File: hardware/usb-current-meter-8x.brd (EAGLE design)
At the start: 94 x 44.5 mm, 154 parts, among them IC10 OPA2234U, IC12 LTC485S, IC2 OPA2234U, IC3 MEGA48/88/168-AU, IC4 OPA2234U, IC5 OPA2234U, IC6 OPA2234U, IC7 OPA2234U, IC8 OPA2234U, IC9 OPA2234U, U3 RJ45-8PTH, X1 MC2, X2 MC2, X3 MC2, X4 MC2, X5 MC2, X6 MC2, X7 MC2, X8 MC2

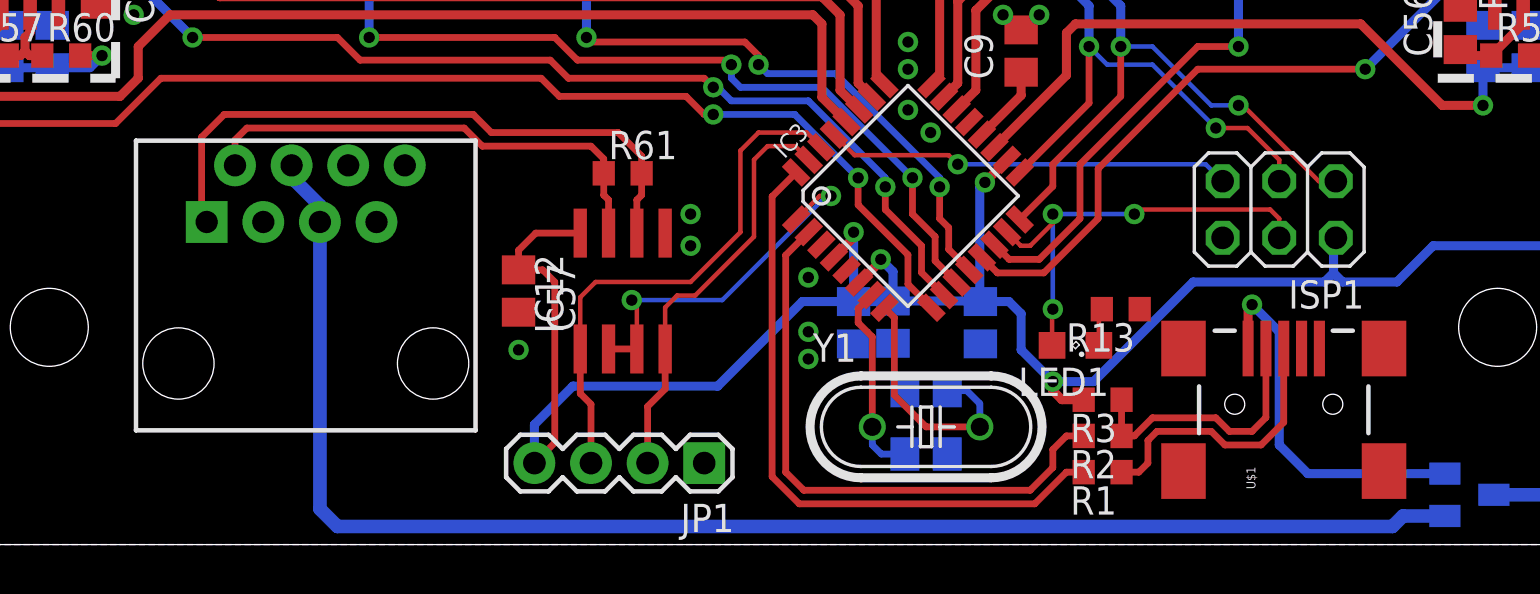
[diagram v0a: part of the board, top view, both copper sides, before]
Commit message: hw: move low-side connector .6mm out
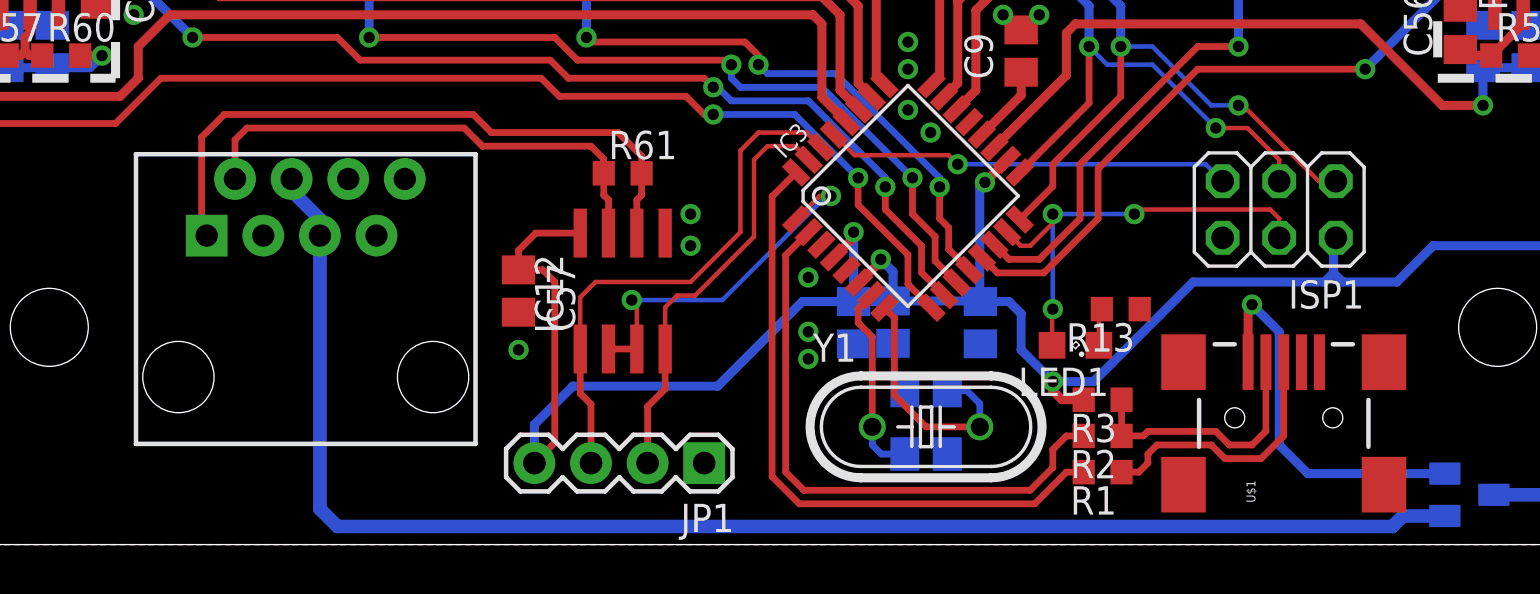
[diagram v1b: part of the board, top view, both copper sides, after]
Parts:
- moved U3 0.61 mm to (26.0, 7.52)
- moved U$1 0.61 mm to (69.9, 5.69)
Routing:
- net VIN_USB: track 16.8 -> 17.4 mm
- net VIN_BUS: track 67.0 -> 66.3 mm
- net N$2: track 12.6 -> 12.0 mm
- net 485_P: track 28.4 -> 29.0 mm
- net 485_N: track 21.9 -> 22.5 mm
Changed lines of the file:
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@@
 <?xml version="1.0" encoding="utf-8"?>
 <!DOCTYPE eagle SYSTEM "eagle.dtd">
-<eagle version="6.1">
+<eagle version="6.2">
 <drawing>
 <settings>
@@
 <element name="R13" library="rcl" package="R0603" value="330" x="62.5856" y="10.5664" rot="R180"/>
 <element name="ISP1" library="balto" package="2X03" value="" x="69.6976" y="15.0368" rot="R180"/>
-<element name="U$1" library="SparkFun" package="USB-MINIB" value="USB-MINIB-5PIN" x="69.9008" y="6.2992" rot="R90"/>
+<element name="U$1" library="SparkFun" package="USB-MINIB" value="USB-MINIB-5PIN" x="69.9008" y="5.6896" rot="R90"/>
 <element name="Y1" library="SparkFun" package="HC49U-V" value="" x="53.848" y="5.2832"/>
 <element name="C9" library="rcl" package="C0805" value=".1u" x="58.1152" y="22.1488" rot="R90"/>
@@
 <element name="C57" library="rcl" package="C0805" value=".1u" x="35.56" y="11.3792" rot="R270"/>
 <element name="R61" library="rcl" package="R0603" value="120" x="40.2336" y="16.6624"/>
-<element name="U3" library="SparkFun-Connectors" package="RJ45-8" value="RJ45-8PTH" x="26.0096" y="8.128"/>
+<element name="U3" library="SparkFun-Connectors" package="RJ45-8" value="RJ45-8PTH" x="26.0096" y="7.5184"/>
 <element name="BOX1" library="hammond" package="1591XXA" value="HAMMOND-BOX-XXA" x="0" y="0"/>
 <element name="D9" library="diode" package="SOT23" value="BAT54C" x="78.232" y="2.2352" rot="MR90"/>
@@
 <contactref element="R3" pad="1"/>
 <contactref element="U$1" pad="D-"/>
-<wire x1="64.008" y1="5.6896" x2="66.8528" y2="5.6896" width="0.3048" layer="1"/>
-<wire x1="66.8528" y1="5.6896" x2="67.4624" y2="5.08" width="0.3048" layer="1"/>
-<wire x1="67.4624" y1="5.08" x2="68.4784" y2="5.08" width="0.3048" layer="1"/>
-<wire x1="68.4784" y1="5.08" x2="69.1008" y2="5.7024" width="0.3048" layer="1"/>
-<wire x1="69.1008" y1="8.7992" x2="69.1008" y2="5.7024" width="0.3048" layer="1"/>
+<wire x1="63.8048" y1="5.08" x2="66.8528" y2="5.08" width="0.3048" layer="1"/>
+<wire x1="66.8528" y1="5.08" x2="67.4624" y2="4.4704" width="0.3048" layer="1"/>
+<wire x1="67.4624" y1="4.4704" x2="68.4784" y2="4.4704" width="0.3048" layer="1"/>
+<wire x1="68.4784" y1="4.4704" x2="69.1008" y2="5.0928" width="0.3048" layer="1"/>
+<wire x1="69.1008" y1="8.1896" x2="69.1008" y2="5.0928" width="0.3048" layer="1"/>
 <wire x1="62.6228" y1="4.8768" x2="62.6228" y2="6.5024" width="0.3048" layer="1"/>
-<wire x1="62.6228" y1="4.8768" x2="63.1952" y2="4.8768" width="0.3048" layer="1"/>
-<wire x1="63.1952" y1="4.8768" x2="64.008" y2="5.6896" width="0.3048" layer="1"/>
+<wire x1="62.6228" y1="4.8768" x2="63.6016" y2="4.8768" width="0.3048" layer="1"/>
+<wire x1="63.6016" y1="4.8768" x2="63.8048" y2="5.08" width="0.3048" layer="1"/>
 </signal>
 <signal name="N$2">
 <contactref element="R1" pad="1"/>
 <contactref element="U$1" pad="D+"/>
-<wire x1="64.2112" y1="5.08" x2="66.6496" y2="5.08" width="0.3048" layer="1"/>
-<wire x1="66.6496" y1="5.08" x2="67.2592" y2="4.4704" width="0.3048" layer="1"/>
-<wire x1="67.2592" y1="4.4704" x2="68.8848" y2="4.4704" width="0.3048" layer="1"/>
-<wire x1="68.8848" y1="4.4704" x2="69.9008" y2="5.4864" width="0.3048" layer="1"/>
-<wire x1="69.9008" y1="8.7992" x2="69.9008" y2="5.4864" width="0.3048" layer="1"/>
-<wire x1="64.2112" y1="5.08" x2="63.8048" y2="4.6736" width="0.3048" layer="1"/>
-<wire x1="63.8048" y1="4.6736" x2="63.8048" y2="3.6576" width="0.3048" layer="1"/>
+<wire x1="64.2112" y1="4.4704" x2="66.6496" y2="4.4704" width="0.3048" layer="1"/>
+<wire x1="66.6496" y1="4.4704" x2="67.2592" y2="3.8608" width="0.3048" layer="1"/>
+<wire x1="67.2592" y1="3.8608" x2="68.8848" y2="3.8608" width="0.3048" layer="1"/>
+<wire x1="68.8848" y1="3.8608" x2="69.9008" y2="4.8768" width="0.3048" layer="1"/>
+<wire x1="69.9008" y1="8.1896" x2="69.9008" y2="4.8768" width="0.3048" layer="1"/>
+<wire x1="64.2112" y1="4.4704" x2="63.8048" y2="4.064" width="0.3048" layer="1"/>
+<wire x1="63.8048" y1="4.064" x2="63.8048" y2="3.6576" width="0.3048" layer="1"/>
 <wire x1="63.8048" y1="3.6576" x2="63.3984" y2="3.2512" width="0.3048" layer="1"/>
 <wire x1="63.3984" y1="3.2512" x2="62.6228" y2="3.2512" width="0.3048" layer="1"/>
@@
 <wire x1="33.528" y1="19.304" x2="22.352" y2="19.304" width="0.3048" layer="1"/>
 <wire x1="22.352" y1="19.304" x2="21.336" y2="18.288" width="0.3048" layer="1"/>
-<wire x1="21.336" y1="18.288" x2="21.336" y2="14.7066" width="0.3048" layer="1"/>
-<wire x1="21.336" y1="14.7066" x2="21.5646" y2="14.478" width="0.3048" layer="1"/>
+<wire x1="21.336" y1="18.288" x2="21.336" y2="14.097" width="0.3048" layer="1"/>
+<wire x1="21.336" y1="14.097" x2="21.5646" y2="13.8684" width="0.3048" layer="1"/>
 </signal>
 <signal name="485_N">
@@
 <wire x1="33.1216" y1="18.6944" x2="23.368" y2="18.6944" width="0.3048" layer="1"/>
 <wire x1="23.368" y1="18.6944" x2="22.8346" y2="18.161" width="0.3048" layer="1"/>
-<wire x1="22.8346" y1="17.018" x2="22.8346" y2="18.161" width="0.3048" layer="1"/>
+<wire x1="22.8346" y1="16.4084" x2="22.8346" y2="18.161" width="0.3048" layer="1"/>
 </signal>
 <signal name="VIN_BUS">
 <contactref element="U3" pad="4"/>
 <contactref element="U3" pad="5"/>
-<wire x1="26.6446" y1="14.478" x2="26.6446" y2="1.6002" width="0.6096" layer="16"/>
+<wire x1="26.6446" y1="13.8684" x2="26.6446" y2="1.6002" width="0.6096" layer="16"/>
 <wire x1="26.6446" y1="1.6002" x2="27.432" y2="0.8128" width="0.6096" layer="16"/>
 <wire x1="27.432" y1="0.8128" x2="74.7776" y2="0.8128" width="0.6096" layer="16"/>
@@
 <wire x1="74.7776" y1="0.8128" x2="75.25" y2="1.2852" width="0.6096" layer="16"/>
 <wire x1="77.132" y1="1.2852" x2="75.25" y2="1.2852" width="0.6096" layer="16"/>
-<wire x1="26.6446" y1="14.478" x2="26.6446" y2="15.2146" width="0.6096" layer="16"/>
-<wire x1="25.3746" y1="17.018" x2="25.3746" y2="16.4846" width="0.6096" layer="16"/>
-<wire x1="25.3746" y1="16.4846" x2="26.6446" y2="15.2146" width="0.6096" layer="16"/>
+<wire x1="26.6446" y1="13.8684" x2="26.6446" y2="14.605" width="0.6096" layer="16"/>
+<wire x1="25.3746" y1="16.4084" x2="25.3746" y2="15.875" width="0.6096" layer="16"/>
+<wire x1="25.3746" y1="15.875" x2="26.6446" y2="14.605" width="0.6096" layer="16"/>
 </signal>
 <signal name="VIN_USB">
 <contactref element="U$1" pad="VBUS"/>
 <contactref element="D9" pad="2"/>
-<wire x1="68.3008" y1="8.7992" x2="68.3008" y2="10.592" width="0.4064" layer="1"/>
+<wire x1="68.3008" y1="8.1896" x2="68.3008" y2="10.592" width="0.4064" layer="1"/>
 <wire x1="68.3008" y1="10.592" x2="68.4784" y2="10.7696" width="0.4064" layer="1"/>
 <via x="68.4784" y="10.7696" extent="1-16" drill="0.508"/>
@@
 </signal>
 </signals>
+<errors>
+</errors>
 </board>
 </drawing>
